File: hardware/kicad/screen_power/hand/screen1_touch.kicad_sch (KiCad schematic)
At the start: 6 parts, among them J101 PI USB, J102 TOUCH, K101 G6K-2P-RF DC5, Q104 2N7000

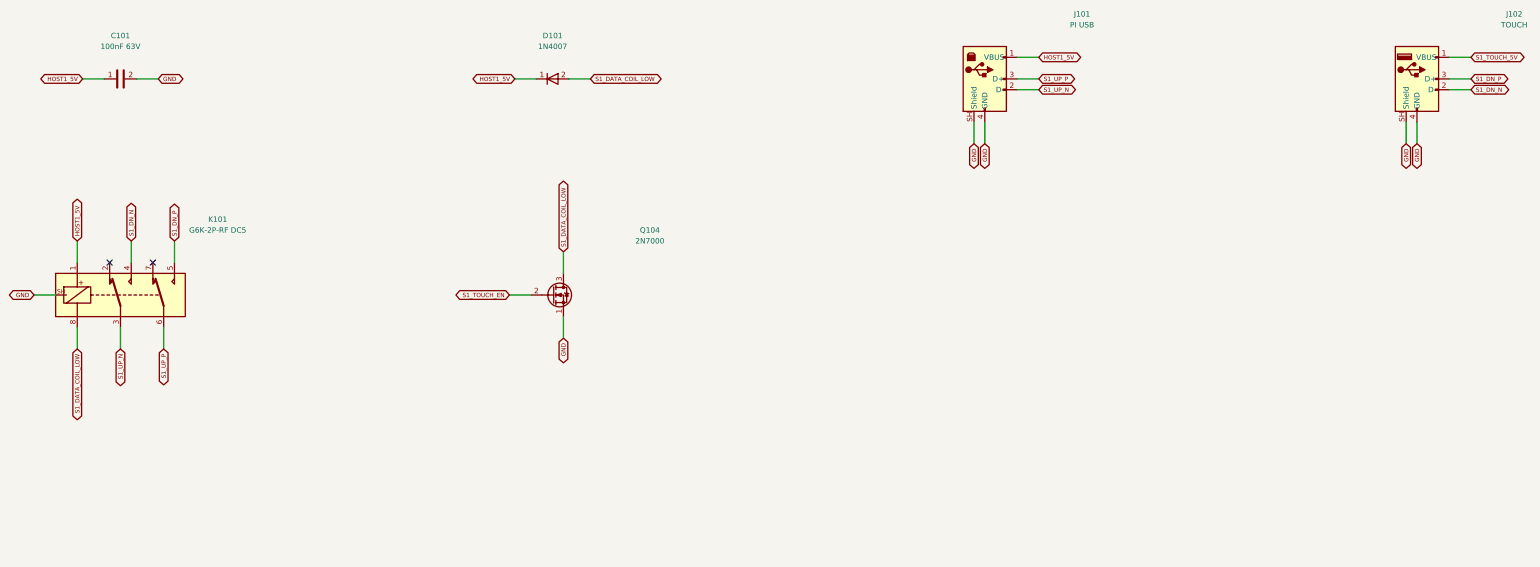
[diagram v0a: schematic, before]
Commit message: refactor(hardware): simplify and compact screen power boards
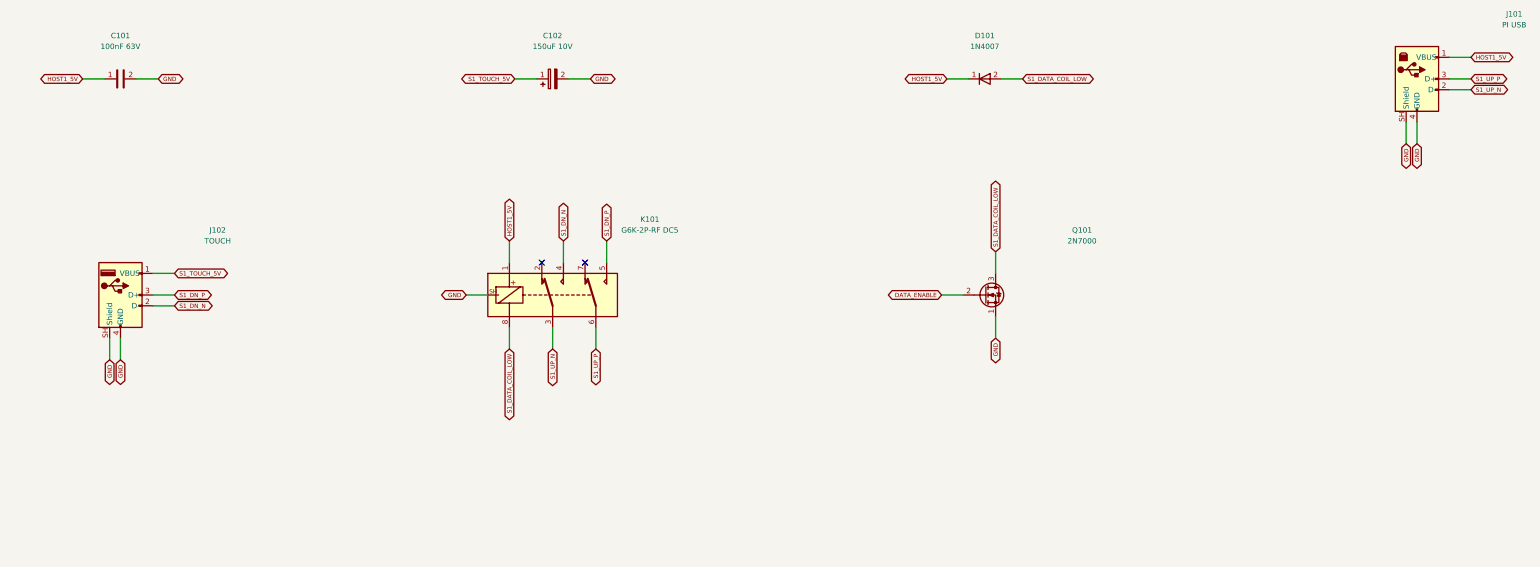
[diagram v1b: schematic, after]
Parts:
- removed Q104: 2N7000, Package_TO_SOT_THT:TO-92_Inline_Wide, symbol screen_symbols:Transistor_FET_2N7000
- added C102: 150uF 10V, Capacitor_THT:CP_Radial_D5.0mm_P2.00mm, symbol screen_symbols:Device_C_Polarized
- added Q101: 2N7000, Package_TO_SOT_THT:TO-92_Inline_Wide, symbol screen_symbols:Transistor_FET_2N7000
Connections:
- net GND: now also C102.2, Q101.1 (S)
- net S1_DATA_COIL_LOW: now also Q101.3 (D)
- net S1_TOUCH_5V: now also C102.1
- new net DATA_ENABLE: Q101.2 (G)
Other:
- moved on the sheet: D101, J101, J102, K101

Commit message: feat(hardware): publish screen switching and board refinements
Add the hand-soldered two-layer screen-power board, aligned console connectors, ADC supply isolation, white ring carrier and reviewed manufacturing ZIPs. Integrate GPIO17 ownership with Weston startup and shutdown; retain assembled-system validation as the hardware gate.
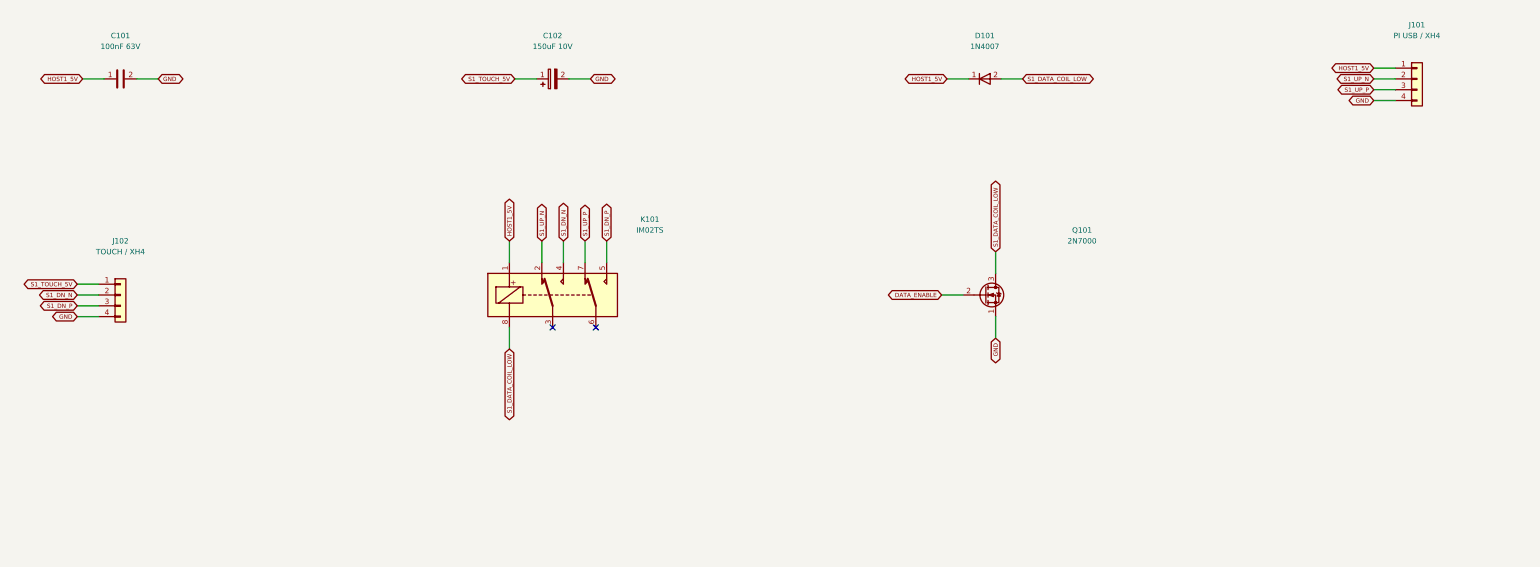
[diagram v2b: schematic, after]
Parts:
- J101: value PI USB -> PI USB / XH4; footprint screen_power:USB_B_Lumberg_2411_06_Horizontal -> Connector_JST:JST_XH_B4B-XH-A_1x04_P2.50mm_Vertical; symbol screen_symbols:screen_power_USB_B_Host -> screen_symbols:Connector_Generic_Conn_01x04; MPN 2411 06 -> B4B-XH-A(LF)(SN)
- J102: value TOUCH -> TOUCH / XH4; footprint Connector_USB:USB_A_Wuerth_614004134726_Horizontal -> Connector_JST:JST_XH_B4B-XH-A_1x04_P2.50mm_Vertical; symbol screen_symbols:Connector_USB_A -> screen_symbols:Connector_Generic_Conn_01x04; MPN 614004134726 -> B4B-XH-A(LF)(SN)
- K101: value G6K-2P-RF DC5 -> IM02TS; footprint screen_power:Relay_DPDT_Omron_G6K-2P-RF -> screen_power:Relay_DPDT_AXICOM_IMSeries_Pitch5.08mm_D0.90mm; symbol screen_symbols:screen_power_G6K-2P-RF -> screen_symbols:Relay_IM03; MPN G6K-2P-RF DC5 -> 1-1462037-3
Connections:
- net GND: no longer J101.SH (Shield), J102.SH (Shield), K101.SH (CASE)
- net S1_UP_N: now also K101.2; no longer K101.3
- net S1_UP_P: now also K101.7; no longer K101.6
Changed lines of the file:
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@@
   (title_block
     (title "Segno screen power / hand / screen1 touch")
-    (rev "B prototype")
-    (comment 1 "Discrete 5V switch. Host VBUS powers only its own RF relay coil.")
+    (rev "G prototype")
+    (comment 1 "Discrete 5V switch. Host VBUS powers only its own signal relay coil.")
     (comment 2 "Physical verification required before release."))
   (wire
@@
   (wire
     (pts
-      (xy 363.22 58.42)
-      (xy 368.3 58.42))
+      (xy 350.52 60.96)
+      (xy 345.44 60.96))
     (stroke
       (width 0)
@@
   (global_label "HOST1_5V"
     (shape bidirectional)
-    (at 368.3 58.42 0)
-    (effects
-      (font
-        (size 1.0 1.0))
-      (justify left))
-)
-  (wire
-    (pts
-      (xy 363.22 66.04)
-      (xy 368.3 66.04))
+    (at 345.44 60.96 180)
+    (effects
+      (font
+        (size 1.0 1.0))
+      (justify right))
+)
+  (wire
+    (pts
+      (xy 350.52 63.5)
+      (xy 345.44 63.5))
     (stroke
       (width 0)
@@
   (global_label "S1_UP_N"
     (shape bidirectional)
-    (at 368.3 66.04 0)
-    (effects
-      (font
-        (size 1.0 1.0))
-      (justify left))
-)
-  (wire
-    (pts
-      (xy 363.22 63.5)
-      (xy 368.3 63.5))
+    (at 345.44 63.5 180)
+    (effects
+      (font
+        (size 1.0 1.0))
+      (justify right))
+)
+  (wire
+    (pts
+      (xy 350.52 66.04)
+      (xy 345.44 66.04))
     (stroke
       (width 0)
@@
   (global_label "S1_UP_P"
     (shape bidirectional)
-    (at 368.3 63.5 0)
-    (effects
-      (font
-        (size 1.0 1.0))
-      (justify left))
-)
-  (wire
-    (pts
-      (xy 355.6 73.66)
-      (xy 355.6 78.74))
+    (at 345.44 66.04 180)
+    (effects
+      (font
+        (size 1.0 1.0))
+      (justify right))
+)
+  (wire
+    (pts
+      (xy 350.52 68.58)
+      (xy 345.44 68.58))
     (stroke
       (width 0)
@@
   (global_label "GND"
     (shape bidirectional)
-    (at 355.6 78.74 270)
-    (effects
-      (font
-        (size 1.0 1.0))
-      (justify right))
-)
-  (wire
-    (pts
-      (xy 353.06 73.66)
-      (xy 353.06 78.74))
-    (stroke
-      (width 0)
-      (type default))
-)
-  (global_label "GND"
-    (shape bidirectional)
-    (at 353.06 78.74 270)
+    (at 345.44 68.58 180)
     (effects
       (font
@@
 )
   (symbol
-    (lib_id "screen_symbols:screen_power_USB_B_Host")
+    (lib_id "screen_symbols:Connector_Generic_Conn_01x04")
     (at 355.59999999999997 63.5 0)
     (unit 1)
@@
     (dnp no)
     (property "Reference" "J101"
-      (at 378.46 48.260000000000005 0)
-      (effects
-        (font
-          (size 1.27 1.27))))
-    (property "Value" "PI USB"
-      (at 378.46 50.800000000000004 0)
-      (effects
-        (font
-          (size 1.27 1.27))))
-    (property "Footprint" "screen_power:USB_B_Lumberg_2411_06_Horizontal"
-      (at 378.46 63.5 0)
-      (effects
-        (font
-          (size 1.27 1.27))
-        (hide yes)))
-    (property "MPN" "2411 06"
-      (at 378.46 63.5 0)
+      (at 355.59999999999997 50.8 0)
+      (effects
+        (font
+          (size 1.27 1.27))))
+    (property "Value" "PI USB / XH4"
+      (at 355.59999999999997 53.339999999999996 0)
+      (effects
+        (font
+          (size 1.27 1.27))))
+    (property "Footprint" "Connector_JST:JST_XH_B4B-XH-A_1x04_P2.50mm_Vertical"
+      (at 355.59999999999997 63.5 0)
+      (effects
+        (font
+          (size 1.27 1.27))
+        (hide yes)))
+    (property "MPN" "B4B-XH-A(LF)(SN)"
+      (at 355.59999999999997 63.5 0)
       (effects
         (font
@@
 )
     (pin "4"
-)
-    (pin SH
 )
     (instances
@@
   (wire
     (pts
-      (xy 58.42 109.22)
-      (xy 63.5 109.22))
+      (xy 45.72 111.76)
+      (xy 40.64 111.76))
     (stroke
       (width 0)
@@
   (global_label "S1_TOUCH_5V"
     (shape bidirectional)
-    (at 63.5 109.22 0)
-    (effects
-      (font
-        (size 1.0 1.0))
-      (justify left))
-)
-  (wire
-    (pts
-      (xy 58.42 116.84)
-      (xy 63.5 116.84))
+    (at 40.64 111.76 180)
+    (effects
+      (font
+        (size 1.0 1.0))
+      (justify right))
+)
+  (wire
+    (pts
+      (xy 45.72 114.3)
+      (xy 40.64 114.3))
     (stroke
       (width 0)
@@
   (global_label "S1_DN_N"
     (shape bidirectional)
-    (at 63.5 116.84 0)
-    (effects
-      (font
-        (size 1.0 1.0))
-      (justify left))
-)
-  (wire
-    (pts
-      (xy 58.42 114.3)
-      (xy 63.5 114.3))
+    (at 40.64 114.3 180)
+    (effects
+      (font
+        (size 1.0 1.0))
+      (justify right))
+)
+  (wire
+    (pts
+      (xy 45.72 116.84)
+      (xy 40.64 116.84))
     (stroke
       (width 0)
@@
   (global_label "S1_DN_P"
     (shape bidirectional)
-    (at 63.5 114.3 0)
-    (effects
-      (font
-        (size 1.0 1.0))
-      (justify left))
-)
-  (wire
-    (pts
-      (xy 50.8 124.46)
-      (xy 50.8 129.54))
+    (at 40.64 116.84 180)
+    (effects
+      (font
+        (size 1.0 1.0))
+      (justify right))
+)
+  (wire
+    (pts
+      (xy 45.72 119.38)
+      (xy 40.64 119.38))
     (stroke
       (width 0)
@@
   (global_label "GND"
     (shape bidirectional)
-    (at 50.8 129.54 270)
-    (effects
-      (font
-        (size 1.0 1.0))
-      (justify right))
-)
-  (wire
-    (pts
-      (xy 48.26 124.46)
-      (xy 48.26 129.54))
-    (stroke
-      (width 0)
-      (type default))
-)
-  (global_label "GND"
-    (shape bidirectional)
-    (at 48.26 129.54 270)
+    (at 40.64 119.38 180)
     (effects
       (font
@@
 )
   (symbol
-    (lib_id "screen_symbols:Connector_USB_A")
+    (lib_id "screen_symbols:Connector_Generic_Conn_01x04")
     (at 50.8 114.3 0)
     (unit 1)
@@
     (dnp no)
     (property "Reference" "J102"
-      (at 73.66 99.06 0)
-      (effects
-        (font
-          (size 1.27 1.27))))
-    (property "Value" "TOUCH"
-      (at 73.66 101.60000000000001 0)
-      (effects
-        (font
-          (size 1.27 1.27))))
-    (property "Footprint" "Connector_USB:USB_A_Wuerth_614004134726_Horizontal"
-      (at 73.66 114.3 0)
-      (effects
-        (font
-          (size 1.27 1.27))
-        (hide yes)))
-    (property "MPN" "614004134726"
-      (at 73.66 114.3 0)
+      (at 50.8 101.6 0)
+      (effects
+        (font
+          (size 1.27 1.27))))
+    (property "Value" "TOUCH / XH4"
+      (at 50.8 104.14 0)
+      (effects
+        (font
+          (size 1.27 1.27))))
+    (property "Footprint" "Connector_JST:JST_XH_B4B-XH-A_1x04_P2.50mm_Vertical"
+      (at 50.8 114.3 0)
+      (effects
+        (font
+          (size 1.27 1.27))
+        (hide yes)))
+    (property "MPN" "B4B-XH-A(LF)(SN)"
+      (at 50.8 114.3 0)
       (effects
         (font
@@
 )
     (pin "4"
-)
-    (pin SH
 )
     (instances
@@
       (justify left))
 )
+  (wire
+    (pts
+      (xy 149.86 106.68)
+      (xy 149.86 101.6))
+    (stroke
+      (width 0)
+      (type default))
+)
+  (global_label "S1_UP_N"
+    (shape bidirectional)
+    (at 149.86 101.6 90)
+    (effects
+      (font
+        (size 1.0 1.0))
+      (justify left))
+)
   (no_connect
-    (at 149.86 106.68)
-)
-  (wire
-    (pts
-      (xy 152.4 121.92)
-      (xy 152.4 127.0))
-    (stroke
-      (width 0)
-      (type default))
-)
-  (global_label "S1_UP_N"
-    (shape bidirectional)
-    (at 152.4 127.0 270)
-    (effects
-      (font
-        (size 1.0 1.0))
-      (justify right))
+    (at 152.4 121.92)
 )
   (wire
@@
       (justify left))
 )
-  (wire
-    (pts
-      (xy 162.56 121.92)
-      (xy 162.56 127.0))
+  (no_connect
+    (at 162.56 121.92)
+)
+  (wire
+    (pts
+      (xy 160.02 106.68)
+      (xy 160.02 101.6))
     (stroke
       (width 0)
@@
   (global_label "S1_UP_P"
     (shape bidirectional)
-    (at 162.56 127.0 270)
-    (effects
-      (font
-        (size 1.0 1.0))
-      (justify right))
-)
-  (no_connect
-    (at 160.02 106.68)
+    (at 160.02 101.6 90)
+    (effects
+      (font
+        (size 1.0 1.0))
+      (justify left))
 )
   (wire
@@
       (justify right))
 )
-  (wire
-    (pts
-      (xy 137.16 114.3)
-      (xy 132.08 114.3))
-    (stroke
-      (width 0)
-      (type default))
-)
-  (global_label "GND"
-    (shape bidirectional)
-    (at 132.08 114.3 180)
-    (effects
-      (font
-        (size 1.0 1.0))
-      (justify right))
-)
   (symbol
-    (lib_id "screen_symbols:screen_power_G6K-2P-RF")
+    (lib_id "screen_symbols:Relay_IM03")
     (at 152.39999999999998 114.3 0)
     (unit 1)
@@
         (font
           (size 1.27 1.27))))
-    (property "Value" "G6K-2P-RF DC5"
+    (property "Value" "IM02TS"
       (at 175.26 99.06 0)
       (effects
         (font
           (size 1.27 1.27))))
-    (property "Footprint" "screen_power:Relay_DPDT_Omron_G6K-2P-RF"
+    (property "Footprint" "screen_power:Relay_DPDT_AXICOM_IMSeries_Pitch5.08mm_D0.90mm"
       (at 175.26 114.3 0)
       (effects
@@
           (size 1.27 1.27))
         (hide yes)))
-    (property "MPN" "G6K-2P-RF DC5"
+    (property "MPN" "1-1462037-3"
       (at 175.26 114.3 0)
       (effects
@@
     (pin "8"
 )
-    (pin SH
-)
     (instances

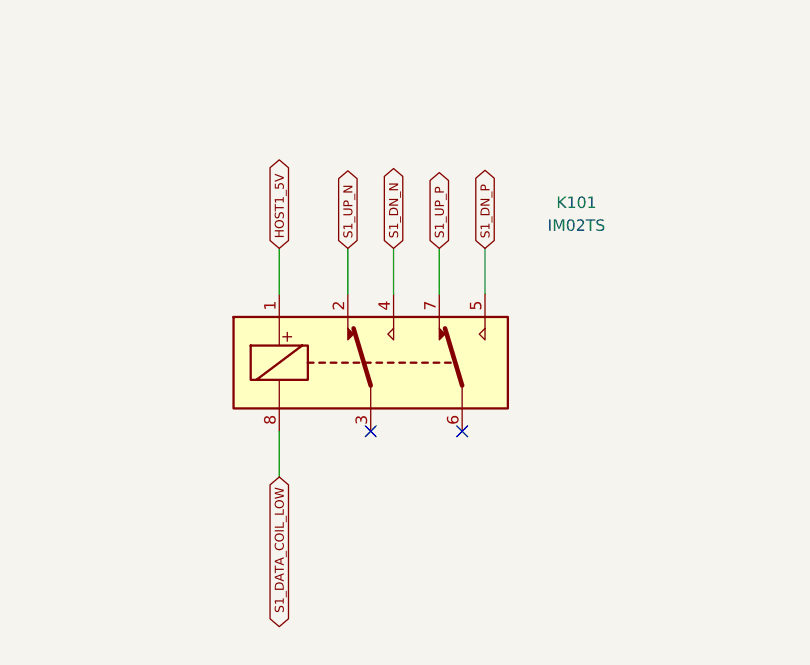
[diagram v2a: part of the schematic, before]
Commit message: fix(hardware): correct screen relay contacts and strengthen power routing
Replace withdrawn Revision I with checked Revision J fabrication files. Correct USB relay commons, reinforce the shared power paths, and verify relay states and a fuse-barrel-independent via path. Record the requested Claude review and independent follow-up checks.
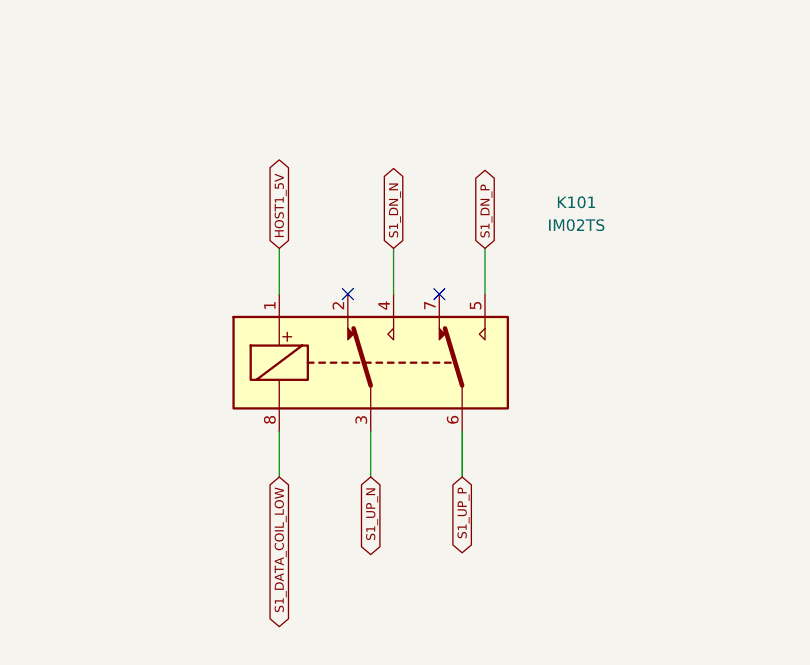
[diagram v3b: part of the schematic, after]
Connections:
- net S1_UP_N: now also K101.3; no longer K101.2
- net S1_UP_P: now also K101.6; no longer K101.7
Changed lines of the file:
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@@
   (title_block
     (title "Segno screen power / hand / screen1 touch")
-    (rev "G prototype")
+    (rev "J prototype")
     (comment 1 "Discrete 5V switch. Host VBUS powers only its own signal relay coil.")
     (comment 2 "Physical verification required before release."))
@@
       (justify left))
 )
-  (wire
-    (pts
-      (xy 149.86 106.68)
-      (xy 149.86 101.6))
+  (no_connect
+    (at 149.86 106.68)
+)
+  (wire
+    (pts
+      (xy 152.4 121.92)
+      (xy 152.4 127.0))
     (stroke
       (width 0)
@@
   (global_label "S1_UP_N"
     (shape bidirectional)
-    (at 149.86 101.6 90)
-    (effects
-      (font
-        (size 1.0 1.0))
-      (justify left))
-)
-  (no_connect
-    (at 152.4 121.92)
+    (at 152.4 127.0 270)
+    (effects
+      (font
+        (size 1.0 1.0))
+      (justify right))
 )
   (wire
@@
       (justify left))
 )
+  (wire
+    (pts
+      (xy 162.56 121.92)
+      (xy 162.56 127.0))
+    (stroke
+      (width 0)
+      (type default))
+)
+  (global_label "S1_UP_P"
+    (shape bidirectional)
+    (at 162.56 127.0 270)
+    (effects
+      (font
+        (size 1.0 1.0))
+      (justify right))
+)
   (no_connect
-    (at 162.56 121.92)
-)
-  (wire
-    (pts
-      (xy 160.02 106.68)
-      (xy 160.02 101.6))
-    (stroke
-      (width 0)
-      (type default))
-)
-  (global_label "S1_UP_P"
-    (shape bidirectional)
-    (at 160.02 101.6 90)
-    (effects
-      (font
-        (size 1.0 1.0))
-      (justify left))
-)
-  (wire
+    (at 160.02 106.68)
+)
+  (wire
